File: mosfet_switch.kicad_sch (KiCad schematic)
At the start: 62 parts, among them J1 Conn_01x06_Pin, Q1 IRFS4310Z, Q10 BCX56, Q11 BCX53, Q12 BCX56, Q13 BCX56, Q14 BCX53, Q15 BCX56, Q2 IRFS4310Z, Q3 IRFS4310Z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

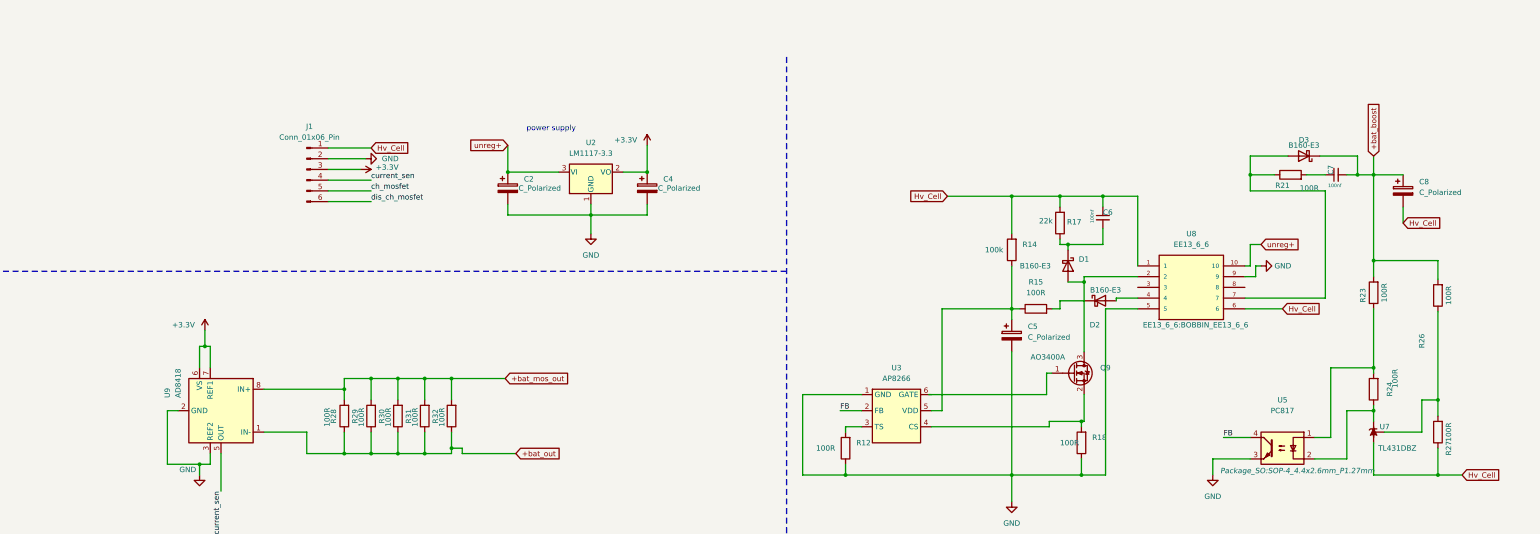
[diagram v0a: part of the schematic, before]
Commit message: [TL431 Circuit] Pick component value
Work on calculating isolated voltage feed back circuitry
changed smps switch mosfet.
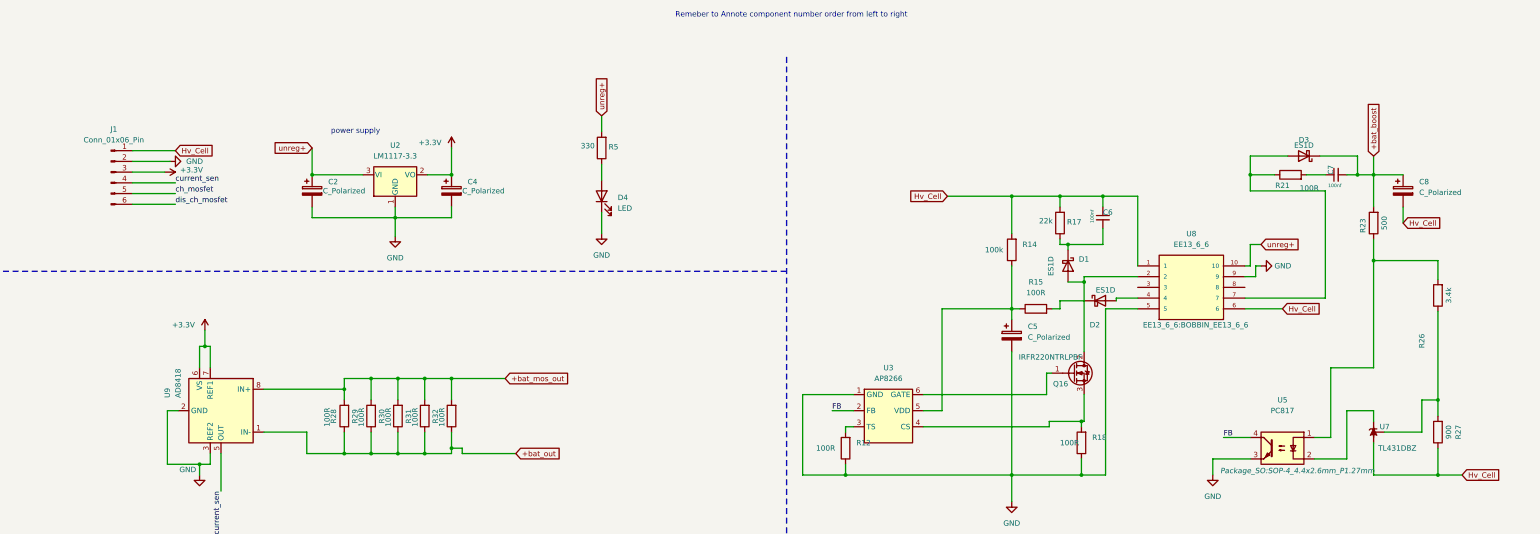
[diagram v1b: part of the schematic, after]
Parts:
- removed Q9: AO3400A, Package_TO_SOT_SMD:SOT-23, symbol Transistor_FET:AO3400A
- removed R24: 100R, Resistor_SMD:R_0402_1005Metric, symbol Device:R
- added D4: LED, LED_SMD:LED_0402_1005Metric, symbol Device:LED
- added Q16: IRFR220NTRLPBF, Package_TO_SOT_SMD:TO-252-2, symbol Transistor_FET:IRFS4310Z
- added R5: 330, Resistor_SMD:R_0402_1005Metric, symbol Device:R
- D1, D2: value B160-E3 -> ES1D; footprint Diode_SMD:D_SOD-123F -> Diode_SMD:D_SMA
- D3: value B160-E3 -> ES1D
- R23: value 100R -> 500
- R26: value 100R -> 3.4k
- R27: value 100R -> 900
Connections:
- net +bat_boost: no longer R26.2
- net GND: now also D4.1 (K)
- net unreg+: now also R5.2
- net at D1.2 (A), U8.2: now also Q16.2 (D)
- net at R23.1, U5.1: now also R26.2
- net at R18.2, U3.4 (CS): now also Q16.3 (S)
- net at U3.6 (GATE): now also Q16.1 (G)
- new net: D4.2 (A), R5.1
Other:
- note added: "Remeber to Annote component number order from left to right"
- moved on the sheet: C2, C4, J1, R23, U2, U3
